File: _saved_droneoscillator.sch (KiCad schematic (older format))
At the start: 48 parts, among them J1 Conn_01x02, J2 Conn_01x03, Q1 BC337, Q2 BC337, Q3 BC337, Q4 BC337, U1 NE5532

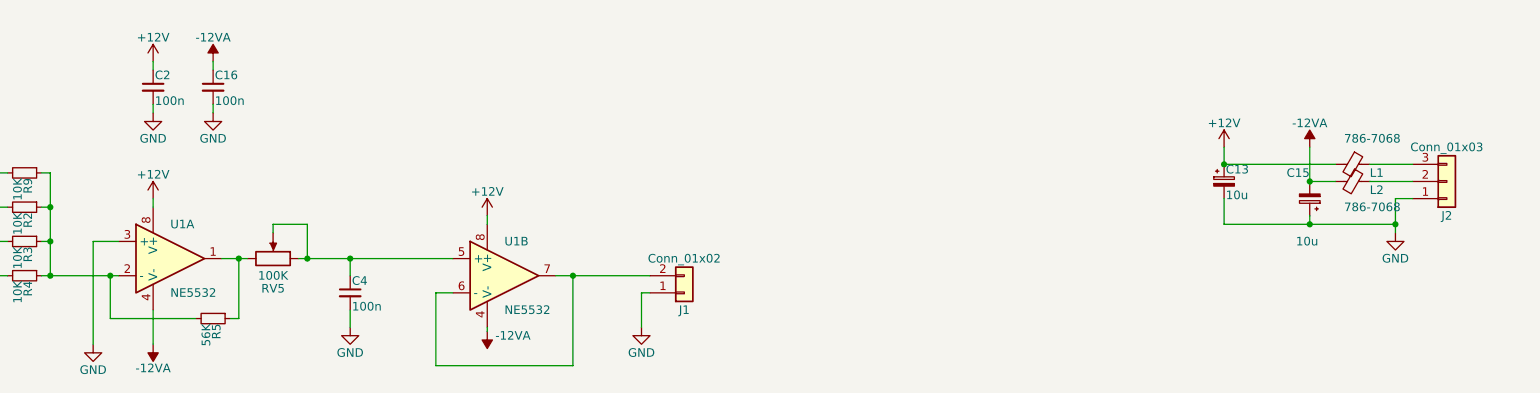
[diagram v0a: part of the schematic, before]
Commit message: Minor schematic changes after prototype build, cleaned up PCB design
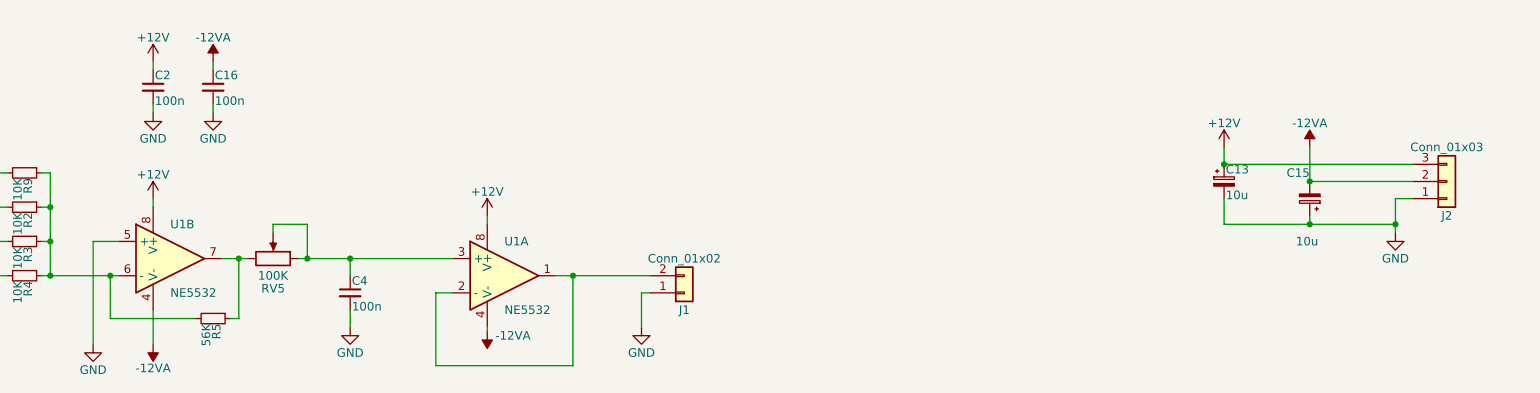
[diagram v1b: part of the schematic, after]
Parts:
- removed L1, L2: 786-7068, Inductor_SMD:L_0805_2012Metric, symbol droneoscillator-rescue:Ferrite_Bead_Small
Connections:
- net +12V: now also J2.3 (Pin_3)
- net -12VA: now also J2.2 (Pin_2)
- net GND: now also U1.5 (+); no longer U1.3 (+)
- net at R5.1, RV5.3: now also U1.7; no longer U1.1
- net at R2.1, R3.1, R4.1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: now also U1.6 (-); no longer U1.2 (-)
- net at C4.1, RV5.1, RV5.2: now also U1.3 (+); no longer U1.5 (+)
- new net: J1.2 (Pin_2), U1.1, U1.2 (-)
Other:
- moved on the sheet: U1A, U1B
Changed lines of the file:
@@
 L droneoscillator-rescue:NE5532 U1
 U 1 1 5B2BA5DA
-P 2250 5150
-F 0 "U1" H 2250 5350 50  0000 L CNN
-F 1 "NE5532" H 2250 4950 50  0000 L CNN
-F 2 "Package_DIP:DIP-8_W7.62mm_Socket_LongPads" H 2250 5150 50  0001 C CNN
-F 3 "" H 2250 5150 50  0001 C CNN
-	1    2250 5150
+P 4200 5250
+F 0 "U1" H 4200 5450 50  0000 L CNN
+F 1 "NE5532" H 4200 5050 50  0000 L CNN
+F 2 "Package_DIP:DIP-8_W7.62mm_Socket_LongPads" H 4200 5250 50  0001 C CNN
+F 3 "" H 4200 5250 50  0001 C CNN
+	1    4200 5250
 	1    0    0    -1
 $EndComp
@@
 L droneoscillator-rescue:NE5532 U1
 U 2 1 5B2BCA1D
-P 4200 5250
-F 0 "U1" H 4200 5450 50  0000 L CNN
-F 1 "NE5532" H 4200 5050 50  0000 L CNN
-F 2 "Package_DIP:DIP-8_W7.62mm_Socket_LongPads" H 4200 5250 50  0001 C CNN
-F 3 "" H 4200 5250 50  0001 C CNN
-	2    4200 5250
+P 2250 5150
+F 0 "U1" H 2250 5350 50  0000 L CNN
+F 1 "NE5532" H 2250 4950 50  0000 L CNN
+F 2 "Package_DIP:DIP-8_W7.62mm_Socket_LongPads" H 2250 5150 50  0001 C CNN
+F 3 "" H 2250 5150 50  0001 C CNN
+	2    2250 5150
 	1    0    0    -1
 $EndComp
@@
 $EndComp
 $Comp
-L droneoscillator-rescue:Ferrite_Bead_Small L1
-U 1 1 5B2C1BEE
-P 9150 4600
-F 0 "L1" V 9200 4700 50  0000 L CNN
-F 1 "786-7068" V 9000 4550 50  0000 L CNN
-F 2 "Inductor_SMD:L_0805_2012Metric" V 9080 4600 50  0001 C CNN
-F 3 "" H 9150 4600 50  0001 C CNN
-	1    9150 4600
-	0    1    1    0
-$EndComp
-$Comp
-L droneoscillator-rescue:Ferrite_Bead_Small L2
-U 1 1 5B2C1C92
-P 9150 4700
-F 0 "L2" V 9200 4800 50  0000 L CNN
-F 1 "786-7068" V 9300 4650 50  0000 L CNN
-F 2 "Inductor_SMD:L_0805_2012Metric" V 9080 4700 50  0001 C CNN
-F 3 "" H 9150 4700 50  0001 C CNN
-	1    9150 4700
-	0    1    1    0
-$EndComp
-$Comp
 L droneoscillator-rescue:CP_Small C13
 U 1 1 5B2C205C
@@
 	9400 4800 9500 4800
 Wire Wire Line
-	9250 4600 9500 4600
-Wire Wire Line
-	9250 4700 9500 4700
-Wire Wire Line
 	8400 4800 8400 4950
 Connection ~ 9400 4950
@@
 Wire Wire Line
 	9400 4950 9400 5000
-Wire Wire Line
-	8900 4700 9050 4700
-Wire Wire Line
-	8400 4600 9050 4600
 Wire Wire Line
 	8900 4950 9400 4950
@@
 	0    -1   -1   0
 $EndComp
+Wire Wire Line
+	8400 4600 9500 4600
+Wire Wire Line
+	8900 4700 9500 4700
 $EndSCHEMATC
